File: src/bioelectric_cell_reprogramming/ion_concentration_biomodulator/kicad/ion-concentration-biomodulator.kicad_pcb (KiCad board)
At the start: 4 copper layers, 96 x 72 mm, 59 parts, among them J1 532610671, J10 39-53-2045, J11 Conn_01x14_Pin, J12 Conn_01x14_Pin, J13 39-53-2045, J14 39-53-2045, J15 Conn_ARM_SWD_TagConnect_TC2030, J16 IPL1-104-01-L-D-K, J17 Conn_01x02_Pin, J18 EJ508A, J19 USB_C_Receptacle_USB2.0_14P, J2 532610671, J20 6620XX11122_66200211122, J21 IPL1-102-01-L-S-K, J3 532610671, J4 532610671, J5 S4B-PH-SM4-TB, J6 Conn_01x02_Pin, J7 6620XX11122_66200211122, J8 39-53-2045, J9 IPL1-102-01-L-S-K, Q1 NDT3055L, Q2 NDT3055L, Q3 NDT3055L, Q4 NDT3055L, Q5 NDT3055L, Q6 NDT3055L, Q7 NDT3055L, SW1 SW_Push, U1 STM32F410CBTx, U2 LM1084-5.0, U3 LM1084-3.3, U4 USBLC6-2SC6

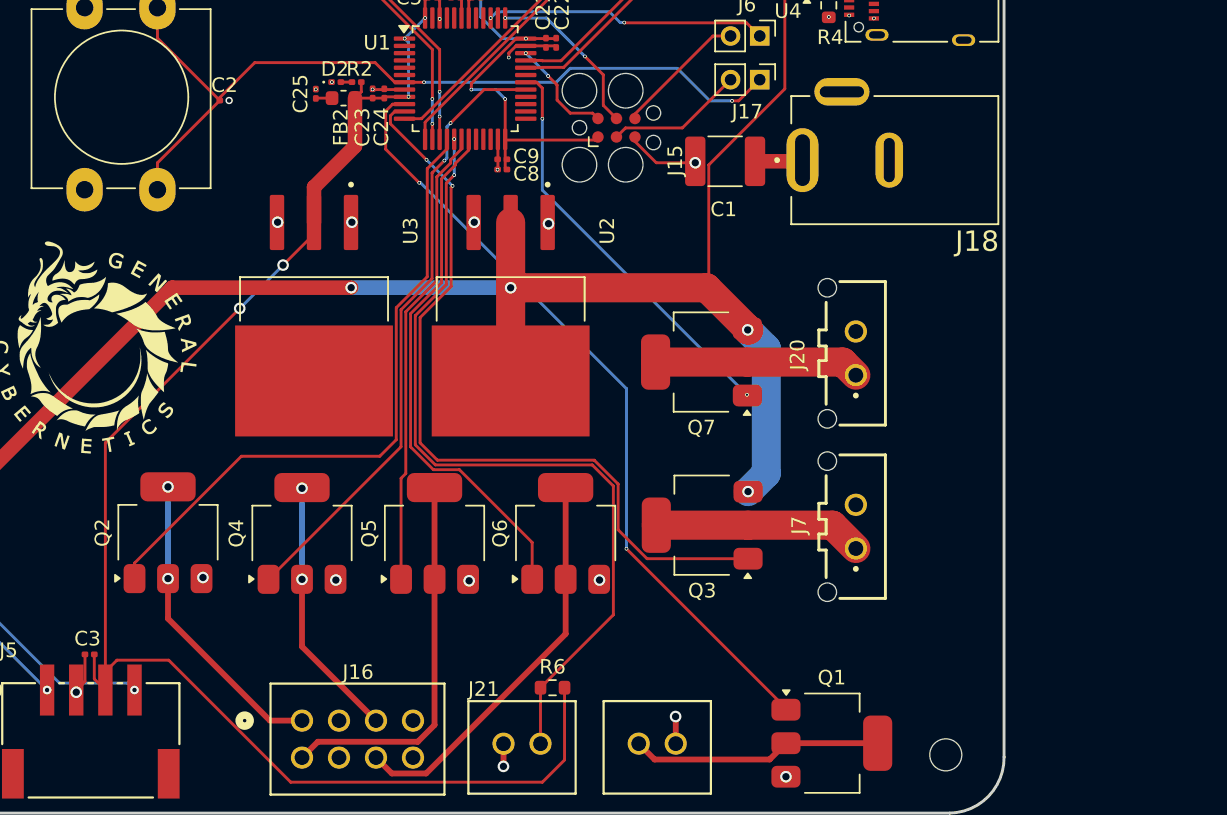
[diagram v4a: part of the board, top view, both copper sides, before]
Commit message: fix: move N-channel FETs from high-side to low-side configuration
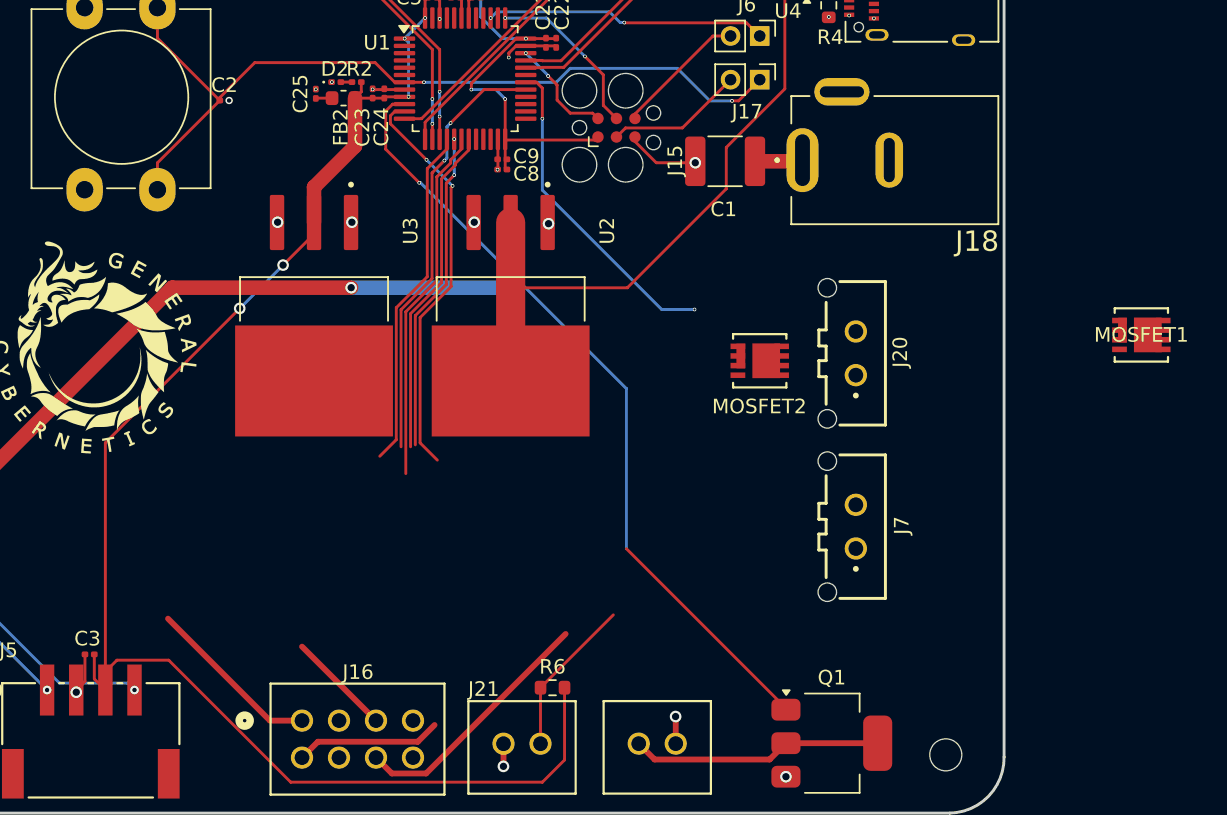
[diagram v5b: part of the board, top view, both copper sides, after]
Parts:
- removed Q2, Q3, Q4, Q5, Q6, Q7: NDT3055L, Package_TO_SOT_SMD:SOT-223-3_TabPin2
- added MOSFET1: BSZ070N08LS5ATMA1, BSZ070N08LS5ATMA1:TSDSON-8-FL_INF, F.Cu at (204.8, 93.5)
- added MOSFET2: BSZ070N08LS5ATMA1, BSZ070N08LS5ATMA1:TSDSON-8-FL_INF, F.Cu at (178.6, 95.3)
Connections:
- J16 pad 2: GND -> +12V
- J16 pad 4: GND -> +12V
- J16 pad 6: GND -> +12V
- J16 pad 8: GND -> +12V
- J20 pad 1: /Fridge Peltier Cooler -> /peltier_coolers/Fridge Peltier Cooler
- J20 pad 2: GND -> +12V
- J7 pad 1: /Peltier Cooler -> /peltier_coolers/Incubator Peltier Cooler
- J7 pad 2: GND -> +12V
- J9 pad 2: GND -> +12V
- Q1 pad 3: +12V -> GND
- U1 pad 11: /PELT_OUT -> /INCUBATOR_PELT_OUT
- U2 pad 4: +5V -> (no net)
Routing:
- net /PELT_OUT: track 53.9 -> 0.00 mm, vias 2 -> 0
- net /INCUBATOR_PELT_OUT: track 0.00 -> 27.9 mm, vias 0 -> 2
- net /THERM_FEEDBACK: track 56.6 -> 33.0 mm
- net /SOL1: track 44.6 -> 23.7 mm
- net +5V: track 138.9 -> 119.3 mm, vias 5 -> 2
- net /SOL_IN3: track 26.3 -> 10.0 mm
- net /Peltier Cooler: track 14.4 -> 0.00 mm
- net /Fridge Peltier Cooler: track 14.1 -> 0.00 mm
- net /SOL4: track 36.4 -> 22.8 mm
- net /SOL2: track 42.6 -> 29.7 mm
- net /SOL_IN2: track 18.1 -> 7.18 mm, vias 2 -> 0
- net /SOL_IN4: track 27.5 -> 17.4 mm
- net /SOL_IN1: track 21.1 -> 12.1 mm, vias 2 -> 0
- net /SOL3: track 31.9 -> 24.5 mm
- net /FRIDGE_PELT_OUT: track 28.2 -> 22.1 mm
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
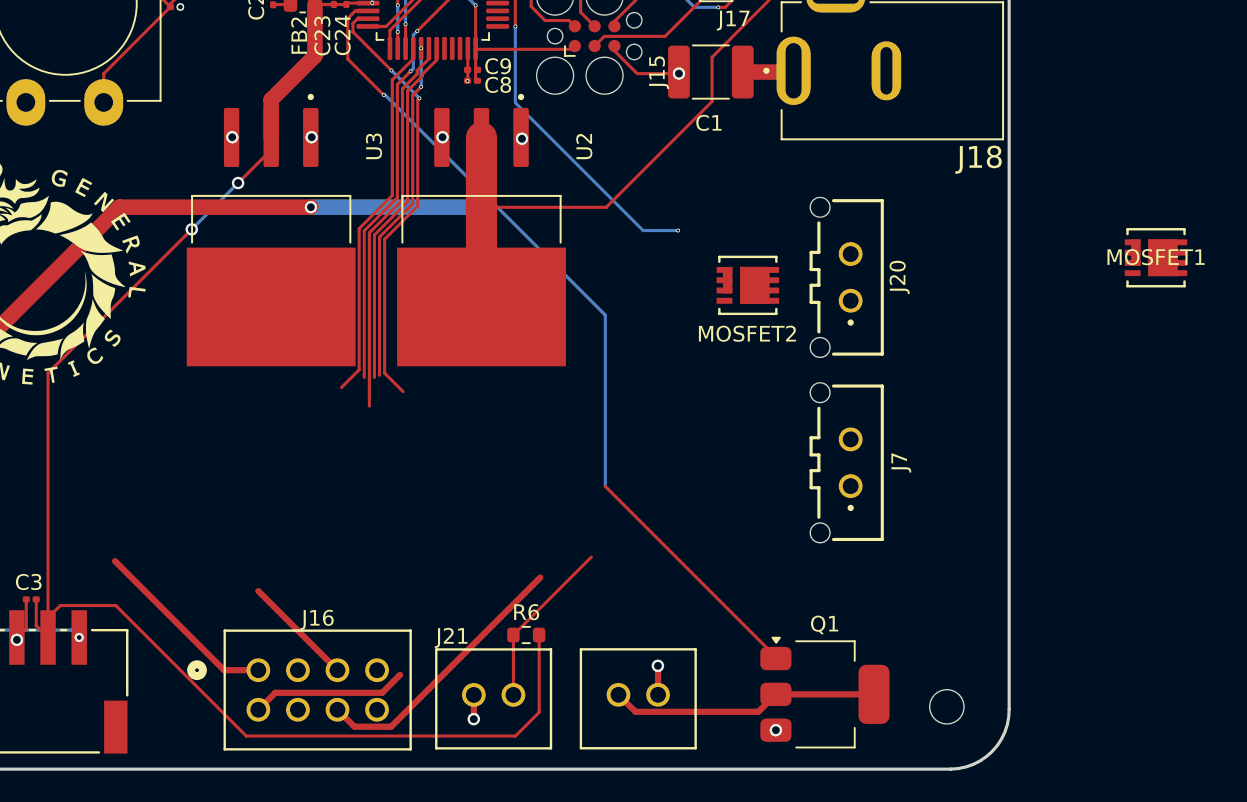
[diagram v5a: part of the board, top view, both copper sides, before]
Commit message: chore: routed MOSFET fixes
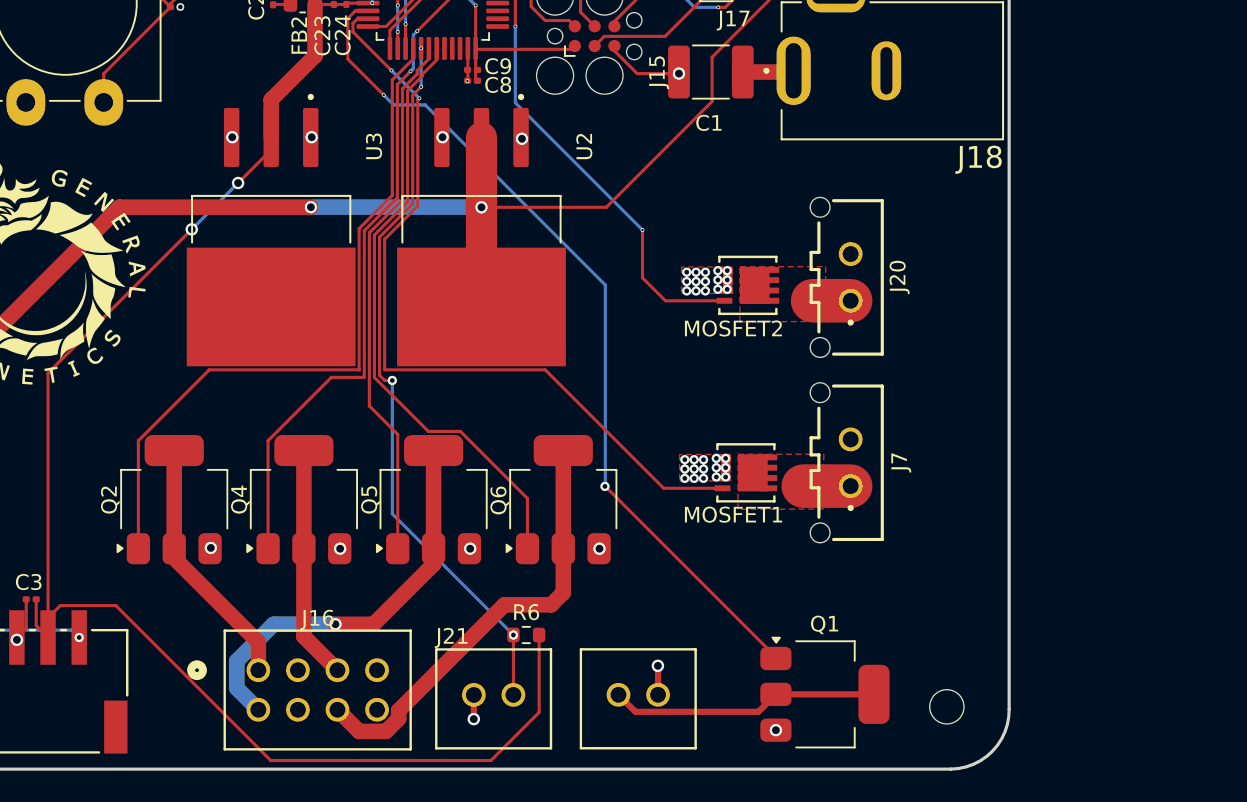
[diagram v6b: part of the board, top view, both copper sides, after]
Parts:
- added Q2: NDT3055L, Package_TO_SOT_SMD:SOT-223-3_TabPin2, F.Cu at (141.8, 109.0)
- added Q4: NDT3055L, Package_TO_SOT_SMD:SOT-223-3_TabPin2, F.Cu at (150.1, 109.0)
- added Q5: NDT3055L, Package_TO_SOT_SMD:SOT-223-3_TabPin2, F.Cu at (158.4, 109.0)
- added Q6: NDT3055L, Package_TO_SOT_SMD:SOT-223-3_TabPin2, F.Cu at (166.8, 109.0)
- moved MOSFET1 29.7 mm to (178.5, 107.3)
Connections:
- MOSFET1 pad 4: /peltier_coolers/INCUBATOR_PELT_OUT -> /INCUBATOR_PELT_OUT
- MOSFET2 pad 4: /peltier_coolers/FRIDGE_PELT_OUT -> /FRIDGE_PELT_OUT
- U2 pad 4: (no net) -> +5V
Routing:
- net /INCUBATOR_PELT_OUT: track 27.9 -> 50.9 mm
- net /SOL1: track 23.7 -> 45.1 mm
- net /SOL4: track 22.8 -> 39.0 mm
- net /SOL_IN3: track 10.0 -> 26.2 mm, vias 0 -> 1
- net /SOL2: track 29.7 -> 44.5 mm
- net /THERM_FEEDBACK: track 33.0 -> 46.5 mm, vias 2 -> 4
- net /SOL_IN4: track 17.4 -> 28.2 mm
- net /SOL3: track 24.5 -> 34.5 mm
- net /SOL_IN2: track 7.18 -> 15.0 mm
- net /FRIDGE_PELT_OUT: track 22.1 -> 28.8 mm
- net /SOL_IN1: track 12.1 -> 16.3 mm
- net /peltier_coolers/Incubator Peltier Cooler: track 0.00 -> 3.04 mm
- net /peltier_coolers/Fridge Peltier Cooler: track 0.00 -> 2.44 mm
- net +3.3V: track 201.0 -> 202.3 mm
- net /SOLEN_OUT: track 54.0 -> 55.2 mm, vias 1 -> 2
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- added copper zone on F.Cu, net /peltier_coolers/Fridge Peltier Cooler
- added copper zone on F.Cu, net /peltier_coolers/Incubator Peltier Cooler
- added copper zone on F.Cu, net GND

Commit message: update mfg files
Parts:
- moved G*** 2.13 mm to (133.5, 96.5)
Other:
- board text added: "v0.0.9"
- board text removed: "BOARD A"
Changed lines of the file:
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@@
 	(footprint "LOGO"
 		(layer "F.Cu")
-		(at 132.99 94.38)
+		(at 133.5 96.45)
 		(property "Reference" "G***"
 			(at 0 0 0)
@@
 		)
 	)
-	(gr_text "BOARD A"
-		(at 109.59 97.75 270)
+	(gr_text "v0.0.9"
+		(at 109.4 100.95 270)
 		(layer "F.SilkS")
 		(effects
@@
 	)
 	(segment
-		(start 181.575 64)
-		(end 183.671001 61.903999)
+		(start 154.2375 78.675)
+		(end 155.425 78.675)
 		(width 0.2)
 		(layer "F.Cu")
@@
 	)
 	(segment
-		(start 170.07917 64)
-		(end 181.575 64)
+		(start 181.575 64)
+		(end 183.671001 61.903999)
 		(width 0.2)
 		(layer "F.Cu")
@@
 	)
 	(segment
-		(start 183.671001 61.903999)
-		(end 183.671001 61.35)
+		(start 170.1 64)
+		(end 181.575 64)
 		(width 0.2)
 		(layer "F.Cu")
@@
 	)
 	(segment
-		(start 155.40417 78.675)
-		(end 170.07917 64)
+		(start 183.671001 61.903999)
+		(end 183.671001 61.35)
 		(width 0.2)
 		(layer "F.Cu")
@@
 	)
 	(segment
-		(start 154.2375 78.675)
-		(end 155.40417 78.675)
+		(start 155.425 78.675)
+		(end 170.1 64)
 		(width 0.2)
 		(layer "F.Cu")

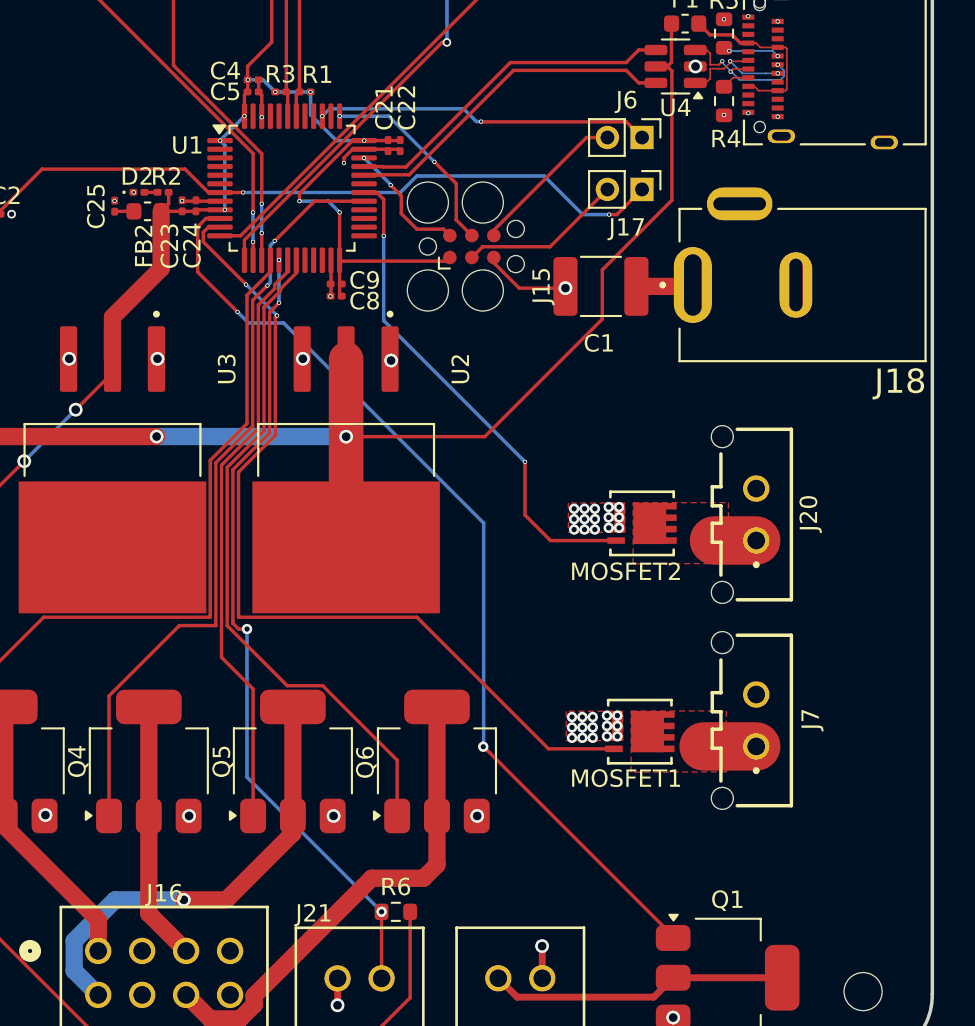
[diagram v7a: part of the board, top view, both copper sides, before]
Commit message: fix: replace fridge peltier cooler FET with an h-bridge
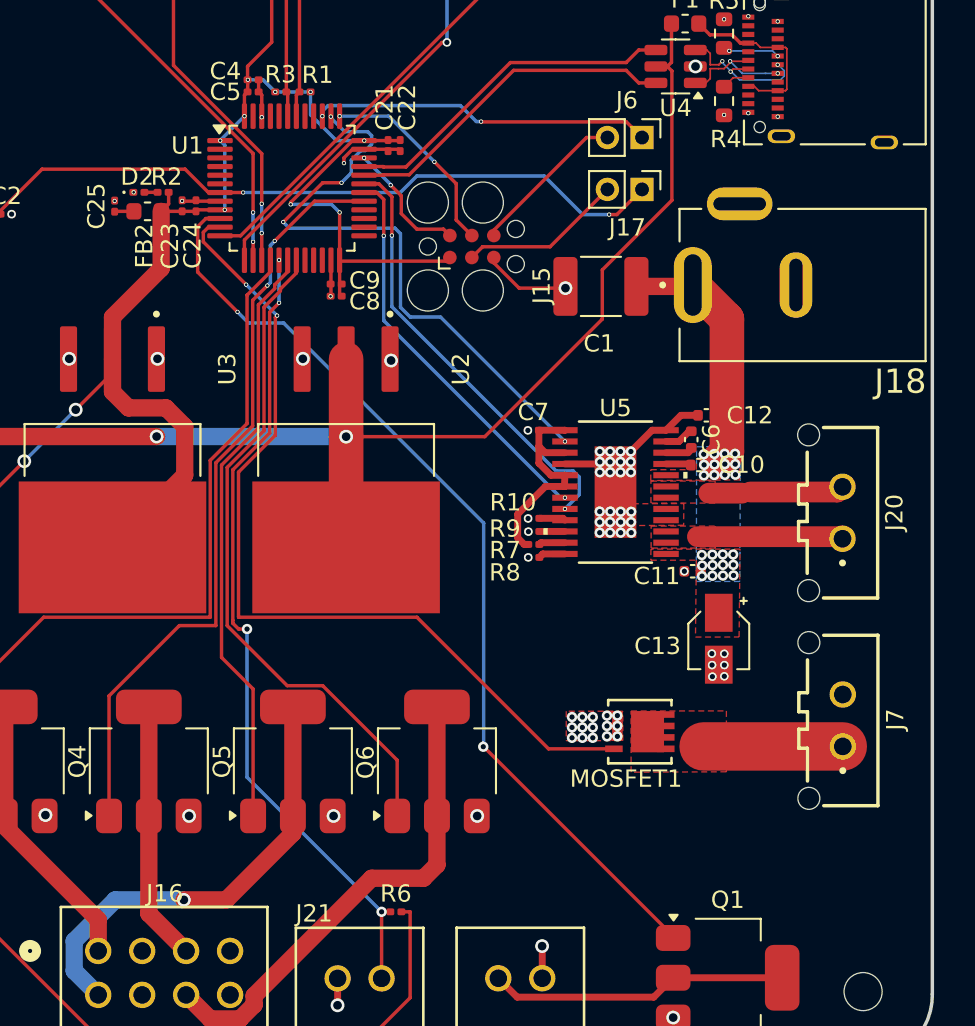
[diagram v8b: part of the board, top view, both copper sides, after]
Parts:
- removed MOSFET2: BSZ070N08LS5ATMA1, BSZ070N08LS5ATMA1:TSDSON-8-FL_INF
- added C10: 1uF, Capacitor_SMD:C_0402_1005Metric, F.Cu at (181.9, 91.9)
- added C11: 100nF, Capacitor_SMD:C_0402_1005Metric, F.Cu at (181.6, 98.1)
- added C12: 100nF, Capacitor_SMD:C_0402_1005Metric, F.Cu at (182.3, 89.0)
- added C13: 10uF, Capacitor_SMD:CP_Elec_3x5.3, F.Cu at (183.1, 102.0)
- added C6: 47nF, Capacitor_SMD:C_0402_1005Metric, F.Cu at (181.5, 90.5)
- added C7: 1uF, Capacitor_SMD:C_0201_0603Metric, F.Cu at (172.3, 89.9)
- added R10: 1K, Resistor_SMD:R_0201_0603Metric, F.Cu at (172.4, 95.0)
- added R7: 10K, Resistor_SMD:R_0201_0603Metric, F.Cu at (172.4, 96.5)
- added R8: 1.5K, Resistor_SMD:R_0201_0603Metric, F.Cu at (172.4, 97.3)
- added R9: 1.5K, Resistor_SMD:R_0201_0603Metric, F.Cu at (172.4, 95.8)
- added U5: DRV8873HPWPR, DRV8873HPWPR.pretty:PWP24_TEX, F.Cu at (177.1, 93.5)
- R6: footprint Resistor_SMD:R_0603_1608Metric -> Resistor_SMD:R_0201_0603Metric
- moved J7 5.00 mm to (190.2, 106.7)
- moved J20 4.99 mm to (190.2, 94.7)
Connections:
- J20 pad 1: /peltier_coolers/Fridge Peltier Cooler -> /peltier_coolers/OUT2
- J20 pad 2: +12V -> /peltier_coolers/OUT1
- U1 pad 30: /FRIDGE_PELT_OUT -> /H_BRIDGE_IN1
- U1 pad 31: unconnected-(U1-PA10-Pad31) -> /H_BRIDGE_IN2
- U1 pad 38: unconnected-(U1-PA15-Pad38) -> /H_BRIDGE_FAULT
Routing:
- net /H_BRIDGE_FAULT: track 0.00 -> 34.8 mm, vias 0 -> 4
- net /FRIDGE_PELT_OUT: track 28.8 -> 0.00 mm, vias 2 -> 0
- net /H_BRIDGE_IN2: track 0.00 -> 25.4 mm, vias 0 -> 2
- net /H_BRIDGE_IN1: track 0.00 -> 23.0 mm, vias 0 -> 2
- net +3.3V: track 202.3 -> 219.2 mm
- net /peltier_coolers/DVDD: track 0.00 -> 13.1 mm
- net +12V: track 5.16 -> 16.4 mm, vias 3 -> 27
- net /peltier_coolers/OUT2: track 0.00 -> 8.48 mm
- net /peltier_coolers/OUT1: track 0.00 -> 7.40 mm
- net GND: track 20.5 -> 27.2 mm, vias 66 -> 86
- net /peltier_coolers/Incubator Peltier Cooler: track 3.04 -> 8.04 mm
- net /peltier_coolers/Fridge Peltier Cooler: track 2.44 -> 0.00 mm
- net /peltier_coolers/CPL: track 0.00 -> 1.76 mm
- net /peltier_coolers/CPH: track 0.00 -> 1.63 mm
- net Net-(U5-IPROPI2): track 0.00 -> 1.56 mm
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- added copper zone on B.Cu, net +12V
- added copper zone on F.Cu, net +12V
- added copper zone on F.Cu, net /peltier_coolers/OUT1
- added copper zone on F.Cu, net /peltier_coolers/OUT2
- removed copper zone on F.Cu, net /peltier_coolers/Fridge Peltier Cooler
